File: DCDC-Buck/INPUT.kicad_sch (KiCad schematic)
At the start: 10 parts, among them CN1 STLZ950GH, IC1 LM7815CT

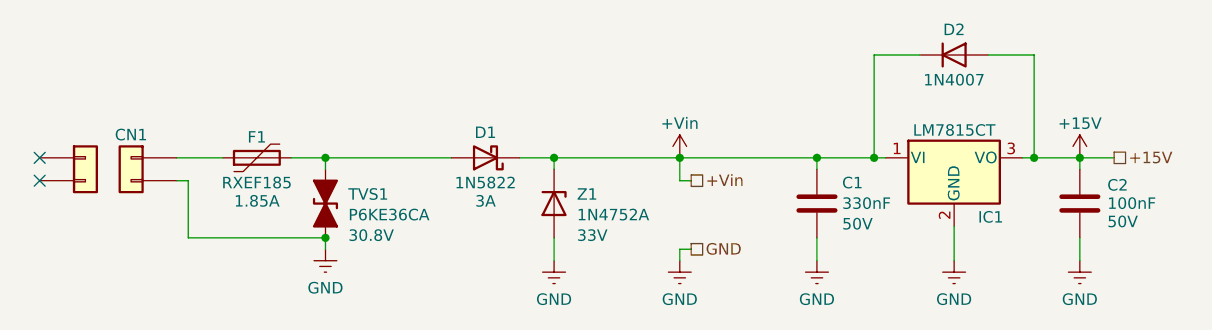
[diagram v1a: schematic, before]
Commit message: Finishing PCB design with 2 layers.
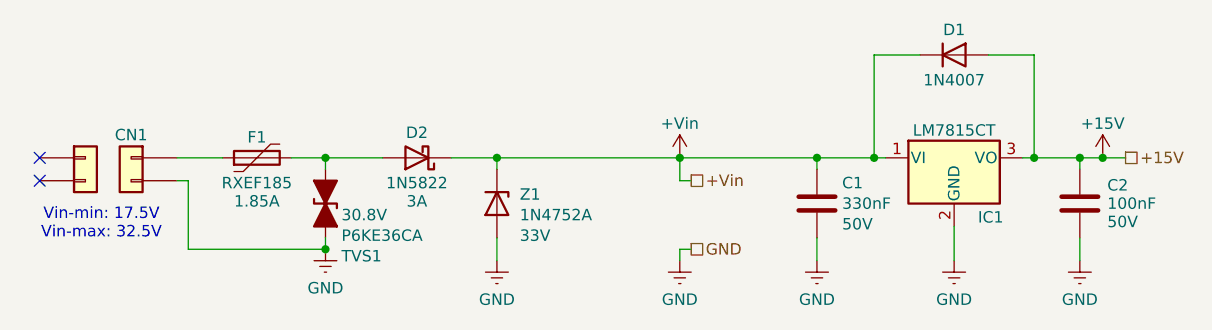
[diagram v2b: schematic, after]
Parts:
- C1: footprint (none) -> Capacitor_THT:C_Disc_D3.0mm_W2.0mm_P2.50mm
- C2: footprint (none) -> Capacitor_THT:C_Disc_D3.0mm_W2.0mm_P2.50mm; Link https://www.multcomercial.com.br/capacitor-multicamada-100k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 -> https://www.multcomercial.com.br/capacitor-ceramico-disco-1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
- renumbered D2 to D1, D1 to D2
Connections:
- net GND: now also TVS1.2 (A2); no longer TVS1.1 (A1)
- net at D2.2 (A), F1.2: now also TVS1.1 (A1); no longer TVS1.2 (A2)
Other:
- note added: "Vin-min: 17.5V Vin-max: 32.5V"
- moved on the sheet: D2, Z1

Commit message: FInishing BOM and PCB.
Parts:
- C1: footprint Capacitor_THT:C_Disc_D3.0mm_W2.0mm_P2.50mm -> Capacitor_THT:C_Rect_L10.0mm_W5.0mm_P5.00mm_P7.50mm
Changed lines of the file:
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@@
 			)
 		)
-		(property "Footprint" "Capacitor_THT:C_Disc_D3.0mm_W2.0mm_P2.50mm"
+		(property "Footprint" "Capacitor_THT:C_Rect_L10.0mm_W5.0mm_P5.00mm_P7.50mm"
 			(at 174.9552 102.87 0)
 			(hide yes)
